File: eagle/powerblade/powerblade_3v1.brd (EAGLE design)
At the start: 25.4 x 25.4 mm, 79 parts, among them J1 JTAG_14PIN_IDC-NL, J2 AC_INF2, J4 TC2030-JLINK-NL, Q1 2N7002, Q4 2SK1829, U1 TPS62122, U2 MCP6V3, U3 MSP430FR5738, U4 NRF51822QF, U6 MAX9910, U7 OPA2369, X1 16MHz, X3 32.768kHz, Y1 UREACH_XTEND

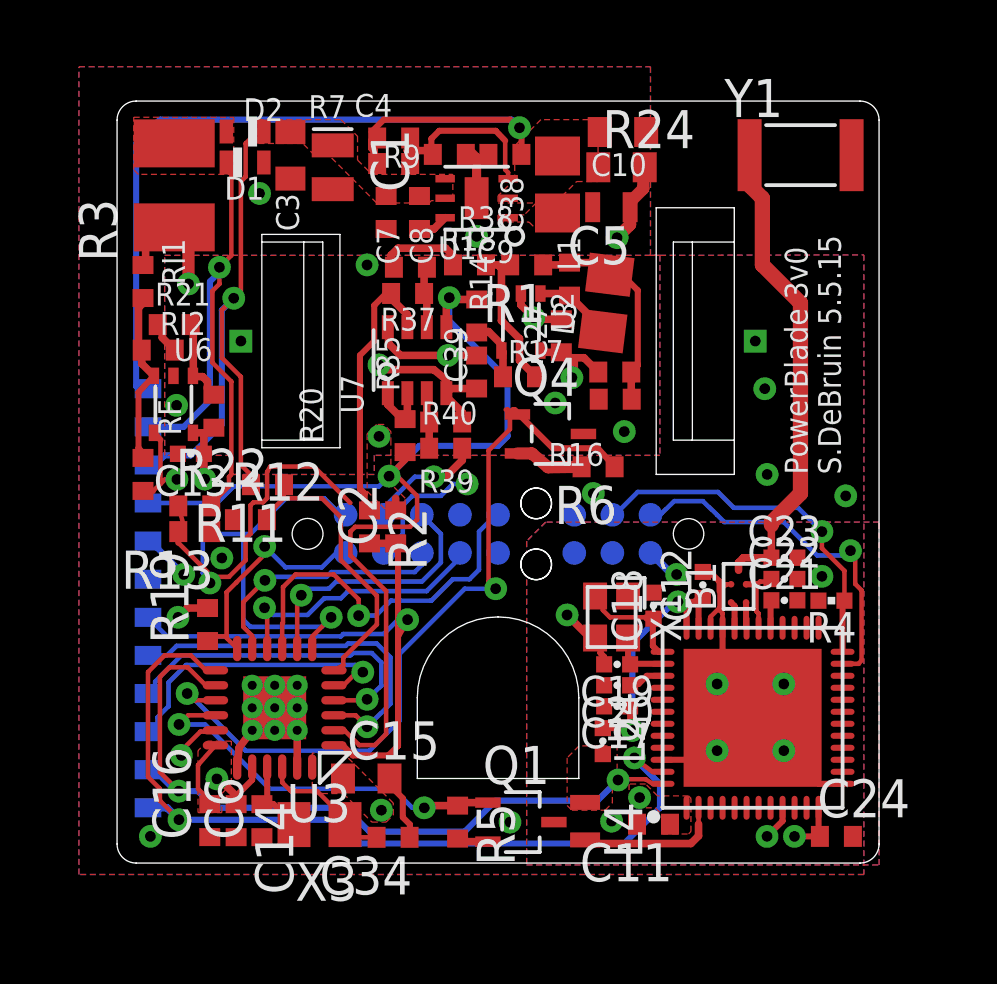
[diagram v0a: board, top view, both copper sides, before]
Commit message: updated tc2050 to no-dim version since co-locating with tc2030 guide pins
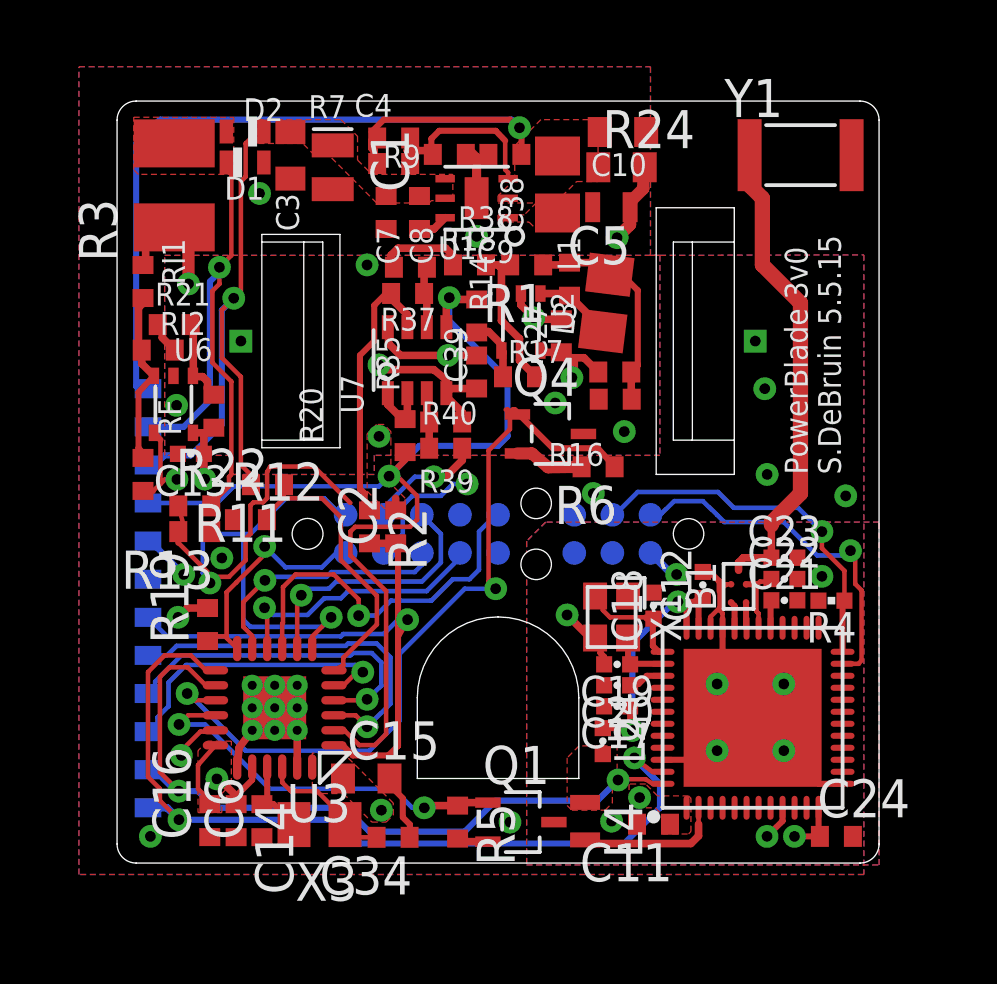
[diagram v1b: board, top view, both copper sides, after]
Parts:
- J1: value JTAG_14PIN_IDC-NL -> JTAG_14PIN_IDC-ND; device ibat:TC2050-IDC-NL-430 -> ibat:TC2050-IDC-NL-430-ND
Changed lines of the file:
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@@
 </element>
 <element name="R19" library="rcl" package="R0402_SM" value="47k" x="-9.68375" y="-9.4488" rot="R90"/>
-<element name="J1" library="ibat" package="TC2050-IDC-NL-430" value="JTAG_14PIN_IDC-NL" x="-2.54" y="-6.4262" rot="MR180">
-<attribute name="TAG-CONNECT" value="TC2050-IDC-NL-430" x="-2.54" y="21.7678" size="1.778" layer="28" rot="MR180" display="off"/>
+<element name="J1" library="ibat" package="TC2050-IDC-NL-430-ND" value="JTAG_14PIN_IDC-ND" x="-2.54" y="-6.4262" rot="MR180">
 <attribute name="DIGIKEY" value="NP" x="-2.54" y="21.7678" size="1.778" layer="28" rot="MR180" display="off"/>
 </element>

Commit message: changed to smaller tabs
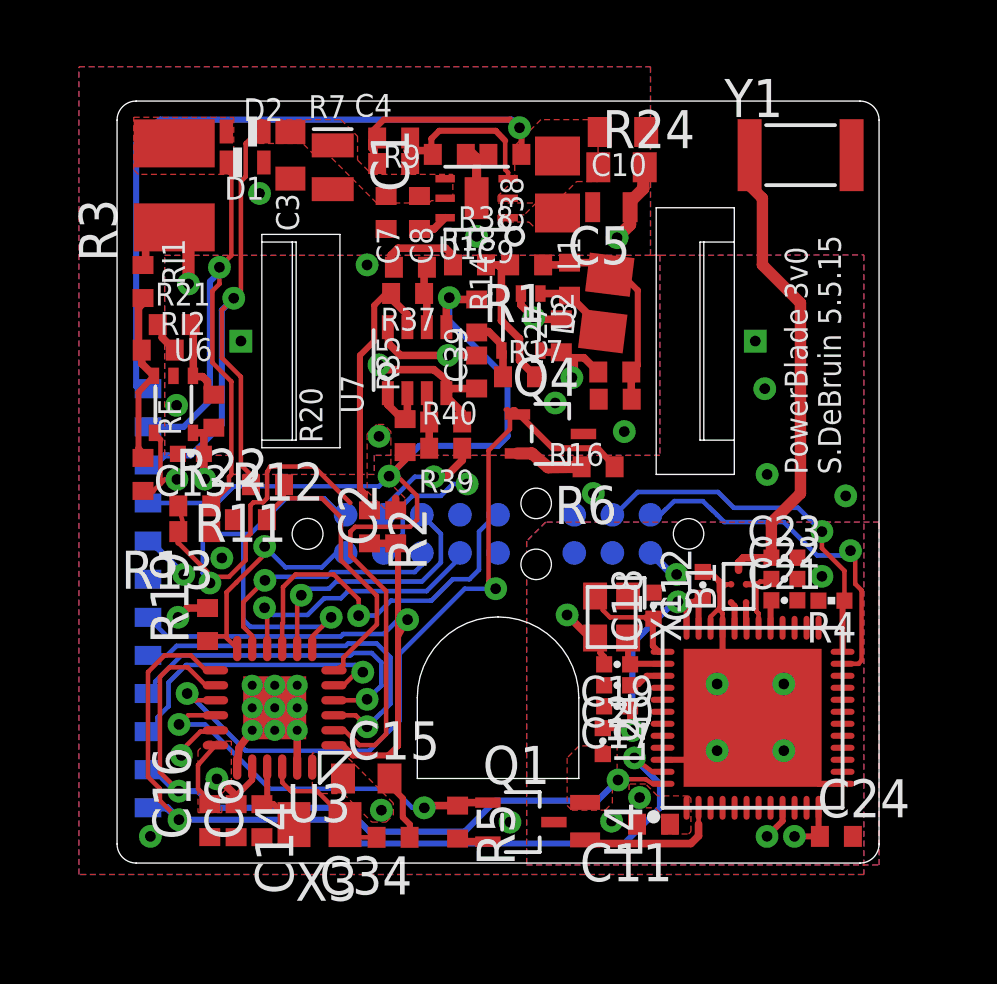
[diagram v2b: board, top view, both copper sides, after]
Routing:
- net VTEST: track 12.9 -> 7.21 mm
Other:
- outline, holes or cut-outs redrawn
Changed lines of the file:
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@@
 <?xml version="1.0" encoding="utf-8"?>
 <!DOCTYPE eagle SYSTEM "eagle.dtd">
-<eagle version="6.3">
+<eagle version="6.5.0">
 <drawing>
 <settings>
@@
 <wire x1="-10.31875" y1="1.905" x2="-10.31875" y2="1.031875" width="1.27" layer="2"/>
 <wire x1="-10.31875" y1="1.031875" x2="-9.286875" y2="0" width="1.27" layer="2"/>
-<wire x1="-8.5725" y1="0" x2="-6.6675" y2="0" width="1.27" layer="2"/>
-<wire x1="-6.6675" y1="1.27" x2="-6.6675" y2="0" width="1.27" layer="2"/>
-<wire x1="-6.6675" y1="0" x2="-6.6675" y2="-2.54" width="1.27" layer="2"/>
 <wire x1="-9.286875" y1="0" x2="-8.5725" y2="0" width="1.27" layer="2"/>
 <wire x1="-11.8364" y1="2.534375" x2="-11.7475" y2="2.623275" width="0.254" layer="1"/>
@@
 <wire x1="8.175625" y1="-7.223125" x2="9.10780625" y2="-7.223125" width="0.254" layer="1"/>
 <wire x1="9.10780625" y1="-7.223125" x2="9.11098125" y2="-7.21995" width="0.254" layer="1"/>
-<wire x1="9.11098125" y1="-7.21995" x2="9.11098125" y2="-6.12901875" width="0.254" layer="1"/>
-<wire x1="9.11098125" y1="-6.12901875" x2="9.11098125" y2="-6.04964375" width="0.508" layer="1"/>
-<wire x1="9.11098125" y1="-6.04964375" x2="10.080625" y2="-5.08" width="0.508" layer="1"/>
-<wire x1="10.080625" y1="-5.08" x2="10.080625" y2="1.27" width="0.508" layer="1"/>
-<wire x1="10.080625" y1="1.27" x2="8.810625" y2="2.54" width="0.508" layer="1"/>
-<wire x1="8.810625" y1="2.54" x2="8.810625" y2="4.7625" width="0.508" layer="1"/>
-<wire x1="8.810625" y1="4.7625" x2="8.41375" y2="5.159375" width="0.508" layer="1"/>
-<wire x1="8.41375" y1="5.159375" x2="8.41375" y2="6.25655" width="0.508" layer="1"/>
+<wire x1="9.11098125" y1="-7.21995" x2="9.11098125" y2="-6.12901875" width="0.381" layer="1"/>
+<wire x1="9.11098125" y1="-6.12901875" x2="9.11098125" y2="-6.04964375" width="0.381" layer="1"/>
+<wire x1="9.11098125" y1="-6.04964375" x2="10.080625" y2="-5.08" width="0.381" layer="1"/>
+<wire x1="10.080625" y1="-5.08" x2="10.080625" y2="1.27" width="0.381" layer="1"/>
+<wire x1="10.080625" y1="1.27" x2="8.810625" y2="2.54" width="0.381" layer="1"/>
+<wire x1="8.810625" y1="2.54" x2="8.810625" y2="4.7625" width="0.381" layer="1"/>
+<wire x1="8.810625" y1="4.7625" x2="8.41375" y2="5.159375" width="0.381" layer="1"/>
+<wire x1="8.41375" y1="5.159375" x2="8.41375" y2="6.25655" width="0.381" layer="1"/>
 <wire x1="8.41375" y1="6.25655" x2="8.3838" y2="6.1976" width="0.508" layer="1"/>
 </signal>

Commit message: changed ble control to pmos, rerouted all but one airwire
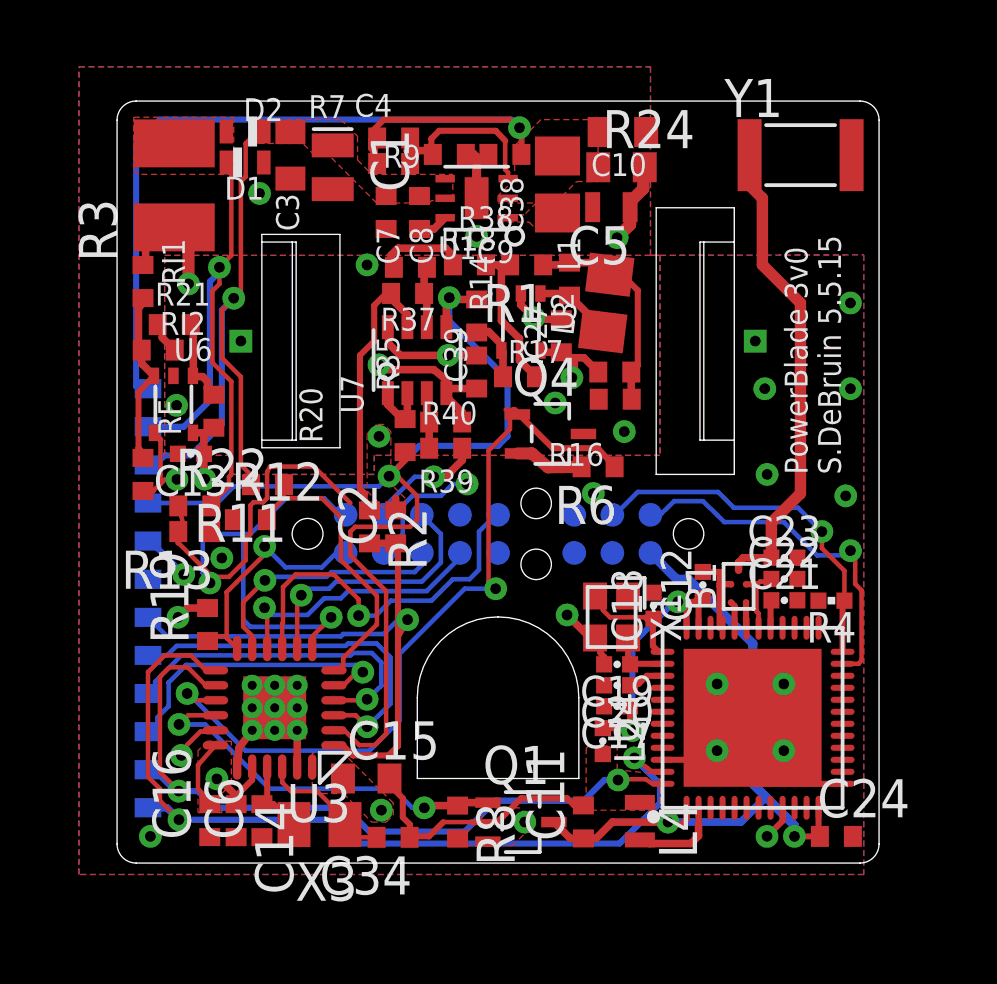
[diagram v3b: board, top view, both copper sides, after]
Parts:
- Q1: value 2N7002 -> NTS4173; device nav:SC-70-3 -> powerfilm:SC-70-3
- moved C11 2.34 mm to (2.84, -16.0), turned to 90 degrees
- moved L4 1.83 mm to (4.73, -16.0)
- renumbered R5 to R8
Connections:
- removed net GND2: B1.GND, C11.2, C12.2, C17.2, C18.2, C19.2, C20.2, C21.2, C22.2, C23.2, C24.2, J4.5, Q1.P3, R4.2, U4.13, U4.33, U4.34, U4.46, U4.GND, X1.2, X1.4
- new net V+: C11.1, C24.1, J4.1, Q1.P3, U4.1, U4.12
- net +3V3: now also Q1.P2, R8.2; no longer C11.1, C24.1, J4.1, U4.1, U4.12
- net GND: now also B1.GND, C11.2, C12.2, C17.2, C18.2, C19.2, C20.2, C21.2, C22.2, C23.2, C24.2, J4.5, R4.2, U4.13, U4.33, U4.34, U4.46, U4.GND, X1.2, X1.4; no longer Q1.P2, R8.2
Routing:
- net V+: track 0.00 -> 22.4 mm, vias 0 -> 2
- net GND: track 15.6 -> 36.0 mm, vias 10 -> 16
- net GND2: track 15.7 -> 0.00 mm, vias 7 -> 0
- net +3V3: track 23.7 -> 20.7 mm, vias 12 -> 10
- net DCC: track 4.85 -> 3.02 mm
- removed copper zone on layer 1, net GND2
- removed copper zone on layer 16, net GND2
- removed copper zone on layer 2, net GND2

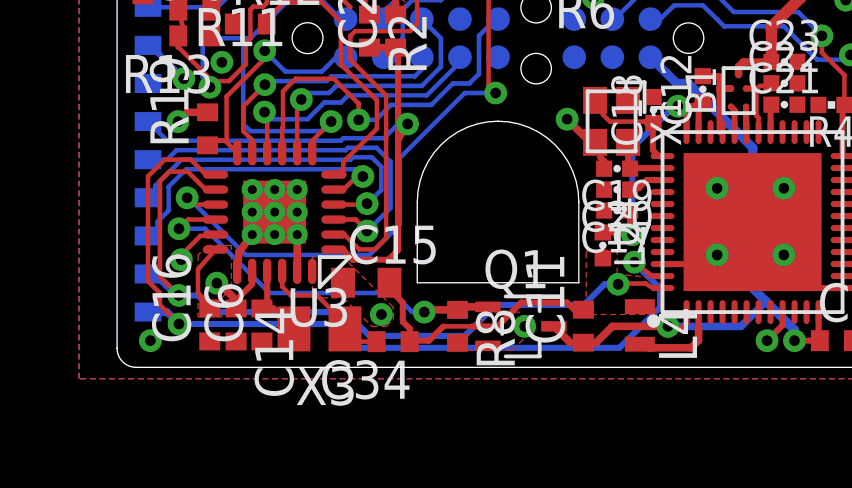
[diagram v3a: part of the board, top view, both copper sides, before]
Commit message: finished routing with 3v3 gate for ble
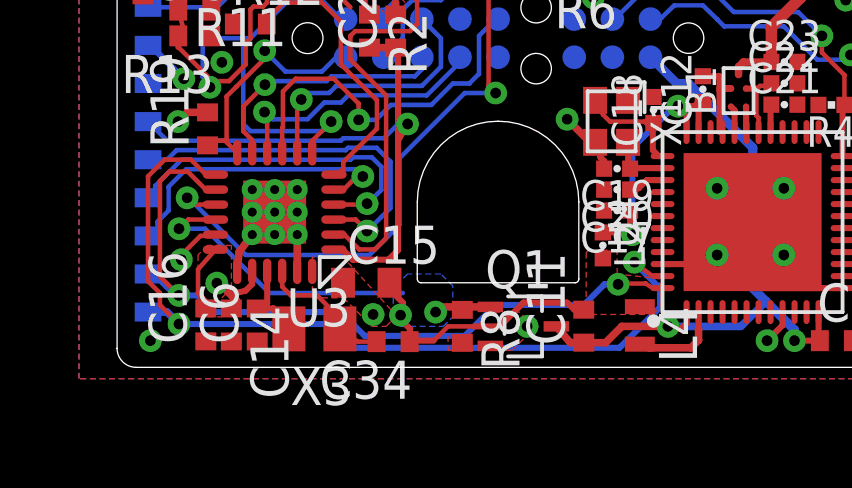
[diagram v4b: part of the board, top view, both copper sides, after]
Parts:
- moved X3 0.17 mm to (-6.12, -16.1)
- moved C14 0.16 mm to (-8.89, -16.0)
- moved R8 0.16 mm to (-1.19, -16.0)
- moved C6 0.16 mm to (-8.03, -16.0)
- moved C16 0.13 mm to (-9.74, -16.0)
- moved Q1 0.08 mm to (0.84, -16.0)
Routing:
- net BLE_ENABLE: track 12.9 -> 11.7 mm
- net GND: vias 16 -> 17
- added copper zone on layer 16, net BLE_ENABLE
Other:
- outline, holes or cut-outs redrawn

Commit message: added block M to powerblade
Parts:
- added U$1: (no value), umich:BLOCK-M
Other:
- board text added: "PowerBlade"
- board text added: "S.DeBruin"
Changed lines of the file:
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@@
 <grid distance="12.5" unitdist="mil" unit="mil" style="lines" multiple="1" display="no" altdistance="3.125" altunitdist="mil" altunit="mil"/>
 <layers>
-<layer number="1" name="Top" color="4" fill="1" visible="yes" active="yes"/>
-<layer number="2" name="Route2" color="1" fill="3" visible="yes" active="yes"/>
+<layer number="1" name="Top" color="4" fill="1" visible="no" active="yes"/>
+<layer number="2" name="Route2" color="1" fill="3" visible="no" active="yes"/>
 <layer number="3" name="Route3" color="4" fill="3" visible="no" active="no"/>
 <layer number="4" name="Route4" color="1" fill="4" visible="no" active="no"/>
@@
 <layer number="13" name="Route13" color="4" fill="5" visible="no" active="no"/>
 <layer number="14" name="Route14" color="1" fill="6" visible="no" active="no"/>
-<layer number="15" name="Route15" color="4" fill="6" visible="yes" active="yes"/>
+<layer number="15" name="Route15" color="4" fill="6" visible="no" active="yes"/>
 <layer number="16" name="Bottom" color="1" fill="1" visible="yes" active="yes"/>
 <layer number="17" name="Pads" color="2" fill="1" visible="yes" active="yes"/>
@@
 <layer number="19" name="Unrouted" color="6" fill="1" visible="yes" active="yes"/>
 <layer number="20" name="Dimension" color="15" fill="1" visible="yes" active="yes"/>
-<layer number="21" name="tPlace" color="7" fill="1" visible="yes" active="yes"/>
+<layer number="21" name="tPlace" color="7" fill="1" visible="no" active="yes"/>
 <layer number="22" name="bPlace" color="7" fill="1" visible="yes" active="yes"/>
-<layer number="23" name="tOrigins" color="15" fill="1" visible="yes" active="yes"/>
+<layer number="23" name="tOrigins" color="15" fill="1" visible="no" active="yes"/>
 <layer number="24" name="bOrigins" color="15" fill="1" visible="yes" active="yes"/>
 <layer number="25" name="tNames" color="7" fill="1" visible="no" active="yes"/>
@@
 <layer number="49" name="Reference" color="7" fill="1" visible="yes" active="yes"/>
 <layer number="50" name="dxf" color="7" fill="1" visible="no" active="no"/>
-<layer number="51" name="tDocu" color="7" fill="1" visible="yes" active="yes"/>
+<layer number="51" name="tDocu" color="7" fill="1" visible="no" active="yes"/>
 <layer number="52" name="bDocu" color="7" fill="1" visible="yes" active="yes"/>
 <layer number="53" name="tGND_GNDA" color="7" fill="9" visible="no" active="no"/>
@@
 <text x="10.31875" y="-4.445" size="0.762" layer="21" rot="R90">PowerBlade 3v0</text>
 <text x="11.43" y="-4.445" size="0.762" layer="21" rot="R90">S.DeBruin 5.5.15</text>
+<text x="6.35" y="5.08" size="1.524" layer="22" rot="MR0">PowerBlade</text>
+<text x="3.4925" y="4.1275" size="0.762" layer="22" rot="MR0">S.DeBruin</text>
 </plain>
 <attributes>
@@
 </element>
 <element name="R8" library="rcl" package="R0402_SM" value="220k" x="-1.190625" y="-16.03375" rot="R270"/>
+<element name="U$1" library="umich" package="BLOCK-M" value="" x="11.1125" y="-10.4775" rot="MR0"/>
 </elements>
 <signals>
